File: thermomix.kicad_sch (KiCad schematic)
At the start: 30 parts, among them J101 DX07S016JA1R1500, J102 Conn_01x05, SW101 SW_Push, SW102 SW_Push, U101 MIC5353-3.3YMT, U102 TPD2E2U06, U103 STM32F303RDTx, Y101 Crystal_GND24

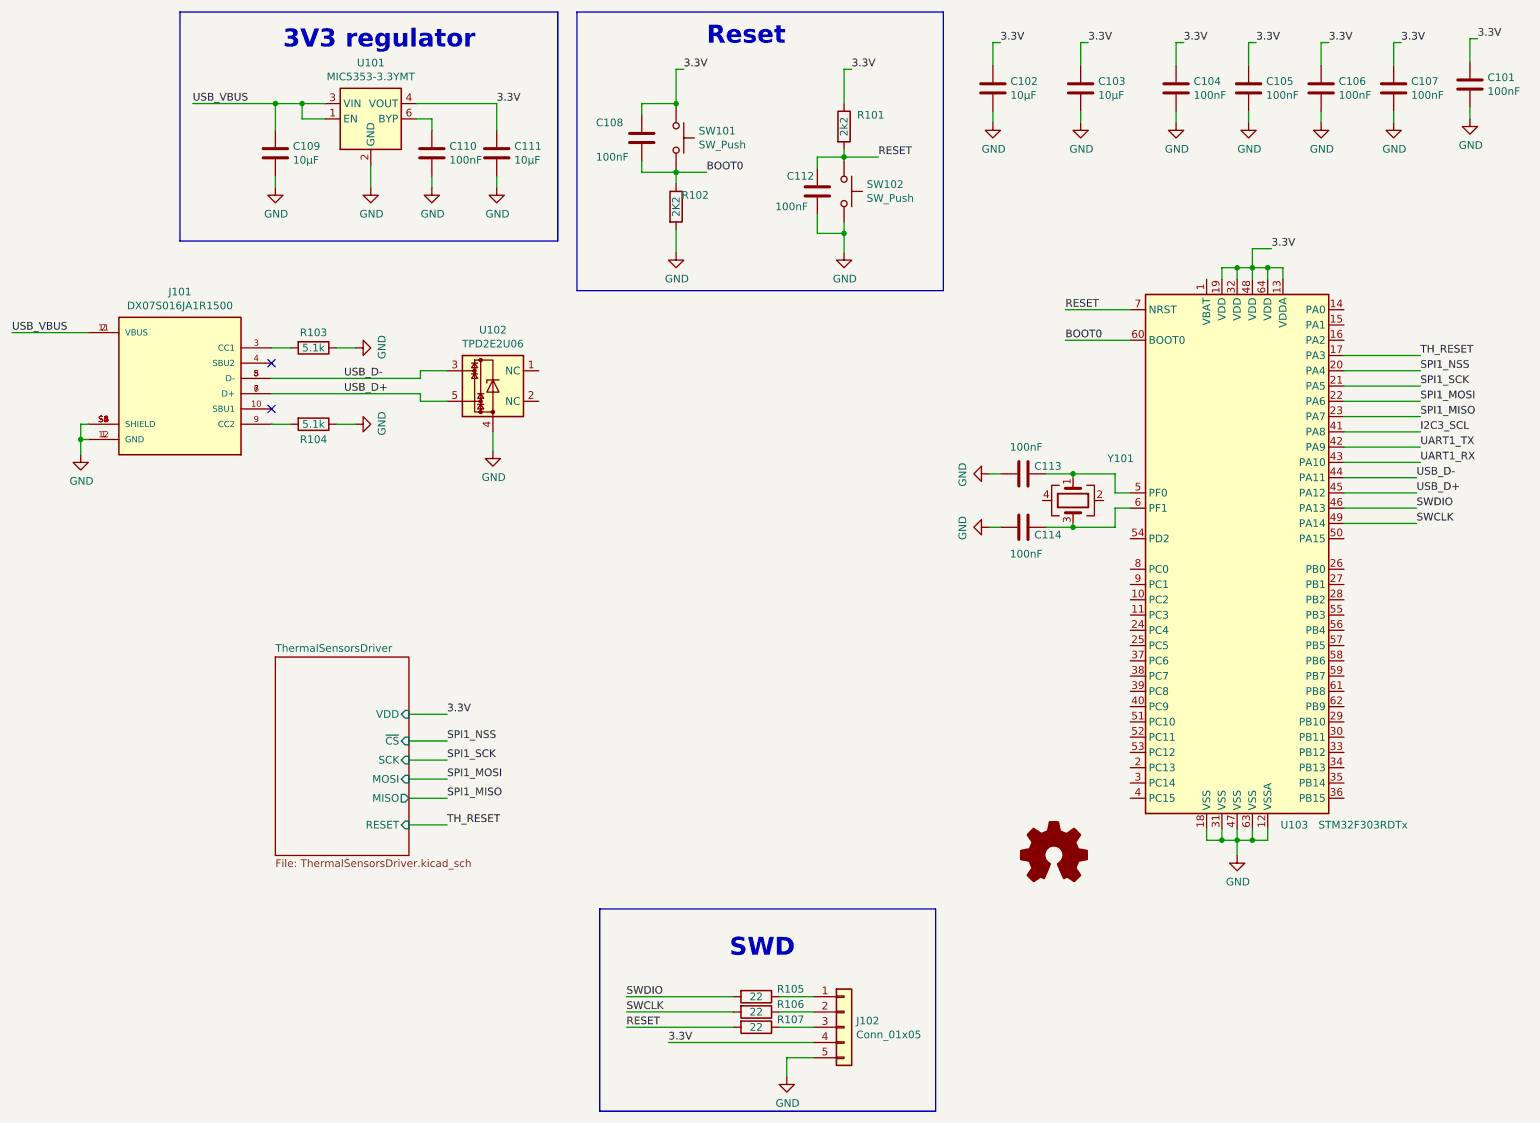
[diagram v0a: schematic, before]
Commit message: Adds sdcard and battery
Signed-off-by: Alexis Jeandet <alexis.jeandet@member.fsf.org>
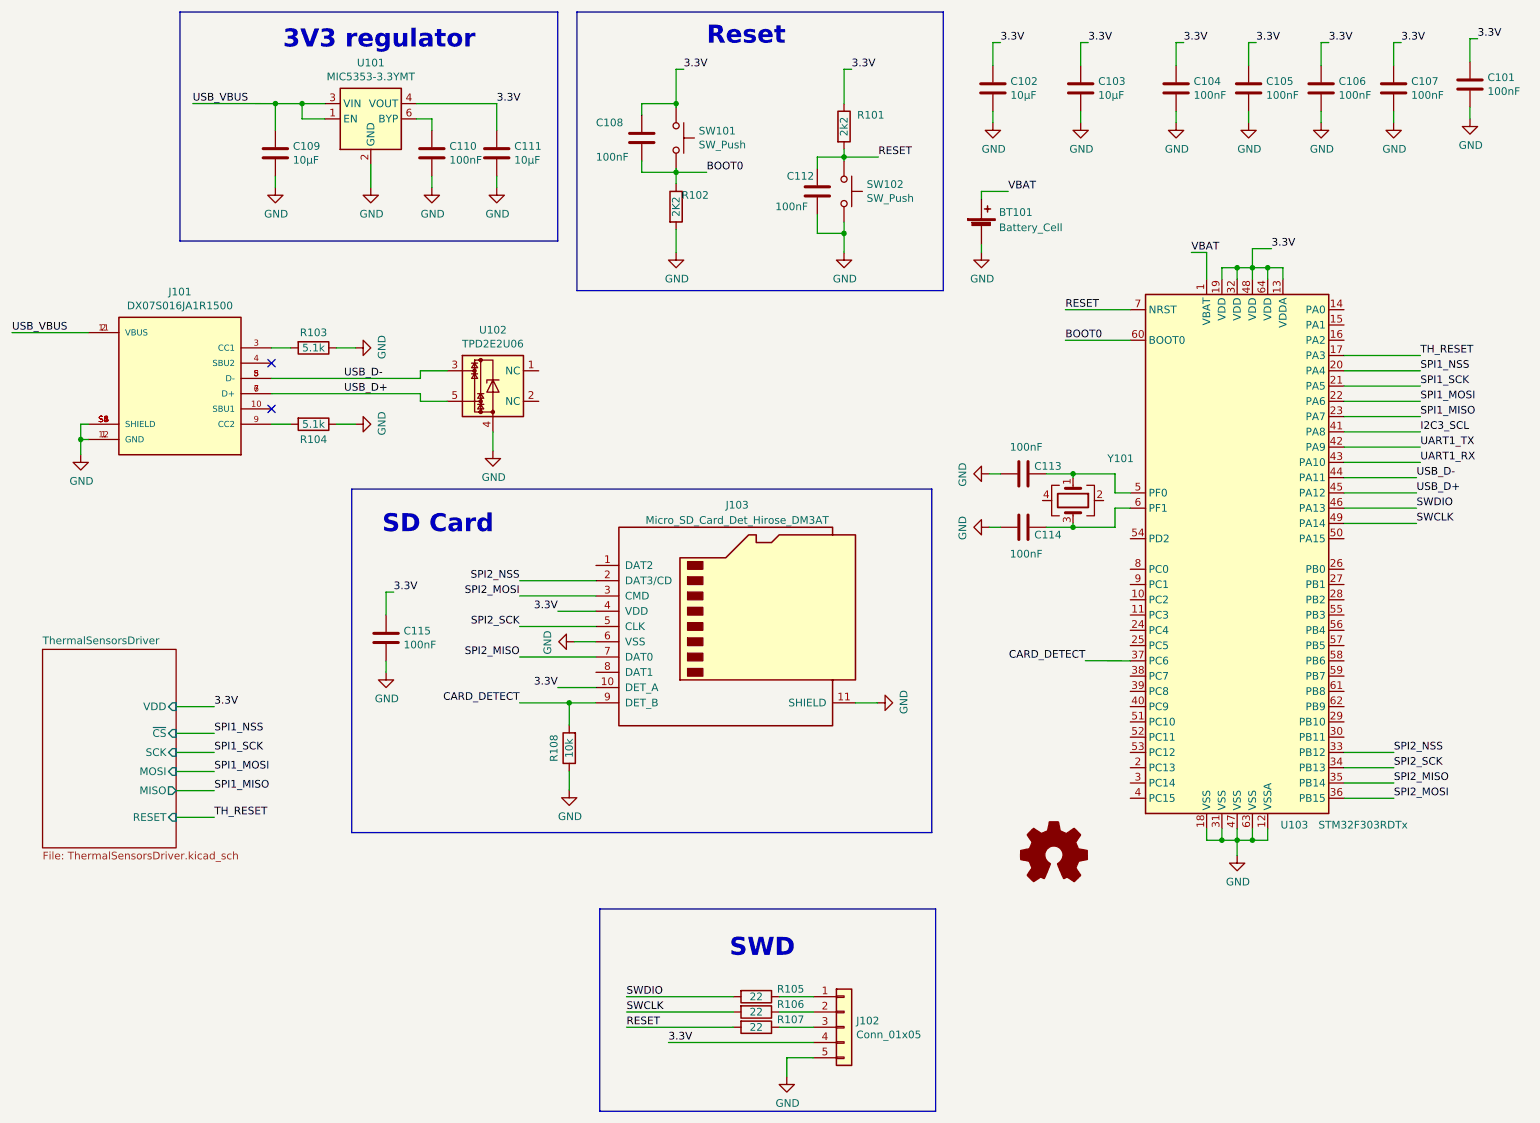
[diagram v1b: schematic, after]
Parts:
- added BT101: Battery_Cell, Battery:BatteryHolder_Keystone_3000_1x12mm, symbol Device:Battery_Cell
- added C115: 100nF, Capacitor_SMD:C_0603_1608Metric_Pad1.08x0.95mm_HandSolder, symbol Device:C
- added J103: Micro_SD_Card_Det_Hirose_DM3AT, Connector_Card:microSD_HC_Hirose_DM3D-SF, symbol Connector:Micro_SD_Card_Det_Hirose_DM3AT
- added R108: 10k, Resistor_SMD:R_0603_1608Metric_Pad0.98x0.95mm_HandSolder, symbol Device:R
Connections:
- net 3.3V: now also C115.1, J103.10 (DET_A), J103.4 (VDD)
- net GND: now also BT101.2 (-), C115.2, J103.11 (SHIELD), J103.6 (VSS), R108.1
- net VBAT: now reaches U103.1 (VBAT)
- net VBAT: now also BT101.1 (+)
- net SPI2_NSS: now reaches U103.33 (PB12)
- net SPI2_NSS: now also J103.2 (DAT3/CD)
- net SPI2_SCK: now reaches U103.34 (PB13)
- net SPI2_SCK: now also J103.5 (CLK)
- net SPI2_MISO: now reaches U103.35 (PB14)
- net SPI2_MISO: now also J103.7 (DAT0)
- net SPI2_MOSI: now reaches U103.36 (PB15)
- net SPI2_MOSI: now also J103.3 (CMD)
- net CARD_DETECT: now reaches U103.37 (PC6)
- net CARD_DETECT: now also J103.9 (DET_B), R108.2
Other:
- note added: "SD Card"

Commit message: 1.0 release
Signed-off-by: Alexis Jeandet <alexis.jeandet@member.fsf.org>
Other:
- company: (none) -> Laboratory of Plasma Physics
- title: (none) -> Thermomix
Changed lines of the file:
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@@
 (kicad_sch (version 20211123) (generator eeschema)
   (paper "A4")
+  (title_block
+    (title "Thermomix")
+    (date "2022-06-03")
+    (rev "1.0")
+    (company "Laboratory of Plasma Physics")
+    (comment 1 "Alexis Jeandet <alexis.jeandet@member.fsf.org>")
+  )
   (junction (at 132.715 29.845) (diameter 0) (color 0 0 0 0)
   )

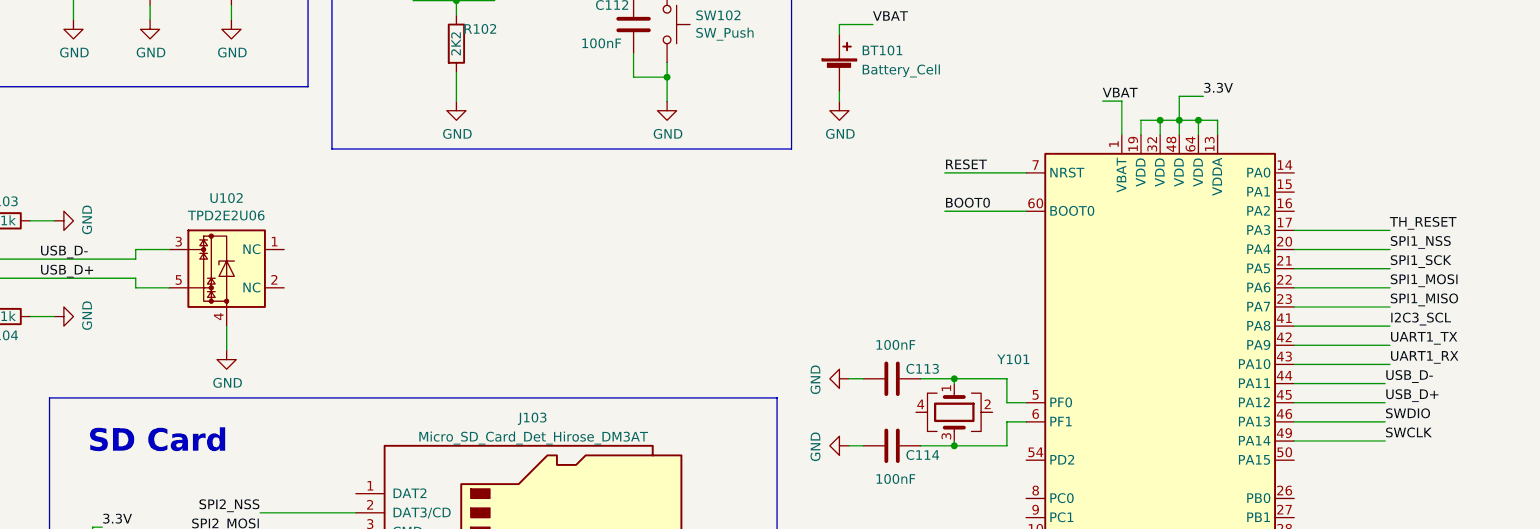
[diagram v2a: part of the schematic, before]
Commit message: Fixes bugs from 1.0
Signed-off-by: Alexis Jeandet <alexis.jeandet@member.fsf.org>
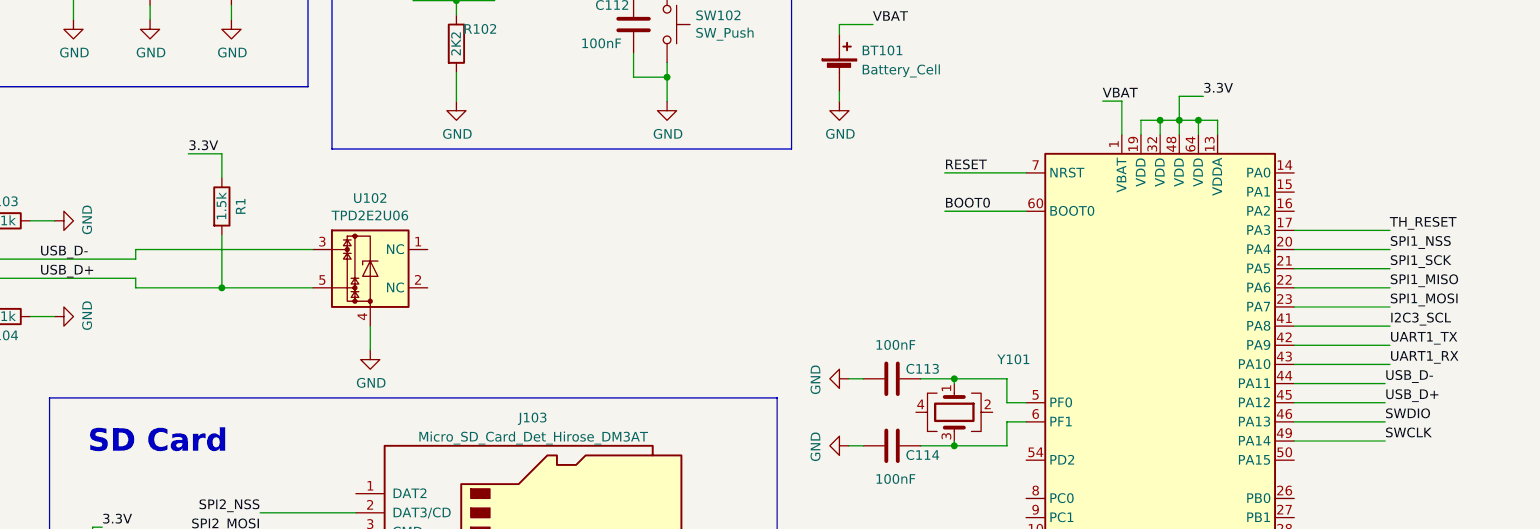
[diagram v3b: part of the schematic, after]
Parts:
- added R1: 1.5k, Resistor_SMD:R_0603_1608Metric_Pad0.98x0.95mm_HandSolder, symbol Device:R
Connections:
- net 3.3V: now also R1.1
- net SPI1_MISO: now also U103.22 (PA6); no longer U103.23 (PA7)
- net SPI1_MOSI: now also U103.23 (PA7); no longer U103.22 (PA6)
- net USB_D+: now also R1.2
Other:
- moved on the sheet: U102
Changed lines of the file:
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@@
     (title "Thermomix")
     (date "2022-06-03")
-    (rev "1.0")
+    (rev "1.1")
     (company "Laboratory of Plasma Physics")
     (comment 1 "Alexis Jeandet <alexis.jeandet@member.fsf.org>")
@@
   )
   (junction (at 231.14 57.15) (diameter 0) (color 0 0 0 0)
+  )
+  (junction (at 101.6 79.375) (diameter 0) (color 0 0 0 0)
   )
   (junction (at 228.6 152.4) (diameter 0) (color 0 0 0 0)
@@
     (stroke (width 0) (type default) (color 0 0 0 0))
   )
-  (wire (pts (xy 102.235 84.455) (xy 102.235 87.63))
+  (wire (pts (xy 121.285 84.455) (xy 121.285 87.63))
     (stroke (width 0) (type default) (color 0 0 0 0))
   )
@@
     (stroke (width 0) (type default) (color 0 0 0 0))
   )
+  (wire (pts (xy 101.6 72.39) (xy 101.6 79.375))
+    (stroke (width 0) (type default) (color 0 0 0 0))
+  )
   (wire (pts (xy 149.86 180.975) (xy 155.575 180.975))
     (stroke (width 0) (type default) (color 0 0 0 0))
@@
     (stroke (width 0) (type default) (color 0 0 0 0))
   )
-  (wire (pts (xy 94.615 79.375) (xy 90.17 79.375))
+  (wire (pts (xy 113.665 79.375) (xy 101.6 79.375))
     (stroke (width 0) (type default) (color 0 0 0 0))
   )
@@
     (stroke (width 0) (type default) (color 0 0 0 0))
   )
+  (wire (pts (xy 101.6 64.77) (xy 101.6 61.595))
+    (stroke (width 0) (type default) (color 0 0 0 0))
+  )
   (wire (pts (xy 227.965 19.685) (xy 227.965 23.495))
     (stroke (width 0) (type default) (color 0 0 0 0))
@@
     (stroke (width 0) (type default) (color 0 0 0 0))
   )
-  (wire (pts (xy 94.615 74.295) (xy 90.17 74.295))
+  (wire (pts (xy 113.665 74.295) (xy 90.17 74.295))
     (stroke (width 0) (type default) (color 0 0 0 0))
   )
@@
     (stroke (width 0) (type default) (color 0 0 0 0))
   )
+  (wire (pts (xy 101.6 61.595) (xy 97.155 61.595))
+    (stroke (width 0) (type default) (color 0 0 0 0))
+  )
   (wire (pts (xy 89.535 29.845) (xy 102.87 29.845))
+    (stroke (width 0) (type default) (color 0 0 0 0))
+  )
+  (wire (pts (xy 101.6 79.375) (xy 90.17 79.375))
     (stroke (width 0) (type default) (color 0 0 0 0))
   )
@@
     (effects (font (size 1.27 1.27)) (justify left bottom))
   )
-  (label "SPI1_MISO" (at 256.54 81.915 0)
+  (label "SPI1_MISO" (at 256.54 79.375 0)
     (effects (font (size 1.27 1.27)) (justify left bottom))
   )
@@
     (effects (font (size 1.27 1.27)) (justify left bottom))
   )
-  (label "SPI1_MOSI" (at 256.54 79.375 0)
+  (label "SPI1_MOSI" (at 256.54 81.915 0)
     (effects (font (size 1.27 1.27)) (justify left bottom))
   )
@@
   )
   (label "3.3V" (at 231.775 53.975 0)
+    (effects (font (size 1.27 1.27)) (justify left bottom))
+  )
+  (label "3.3V" (at 97.155 61.595 0)
     (effects (font (size 1.27 1.27)) (justify left bottom))
   )
@@
     )
     (property "Datasheet" "~" (id 3) (at 185.42 27.305 0)
+      (effects (font (size 1.27 1.27)) hide)
+    )
+    (pin "1")
+    (pin "2")
+  )
+  (symbol (lib_id "Device:R") (at 101.6 68.58 0) (unit 1)
+    (in_bom yes) (on_board yes)
+    (property "Reference" "R1" (id 0) (at 104.14 68.58 90))
+    (property "Value" "1.5k" (id 1) (at 101.6 68.58 90))
+    (property "Footprint" "Resistor_SMD:R_0603_1608Metric_Pad0.98x0.95mm_HandSolder" (id 2) (at 99.822 68.58 90)
+      (effects (font (size 1.27 1.27)) hide)
+    )
+    (property "Datasheet" "~" (id 3) (at 101.6 68.58 0)
       (effects (font (size 1.27 1.27)) hide)
     )
@@
     (pin "S6")
   )
-  (symbol (lib_id "Power_Protection:TPD2E2U06") (at 102.235 76.835 0) (unit 1)
-    (in_bom yes) (on_board yes)
-    (property "Reference" "U102" (id 0) (at 102.235 67.5132 0))
-    (property "Value" "TPD2E2U06" (id 1) (at 102.235 69.8246 0))
-    (property "Footprint" "Package_TO_SOT_SMD:SOT-553" (id 2) (at 81.915 83.185 0)
-      (effects (font (size 1.27 1.27)) hide)
-    )
-    (property "Datasheet" "http://www.ti.com/lit/ds/symlink/tpd2e2u06.pdf" (id 3) (at 97.155 71.755 0)
+  (symbol (lib_id "Power_Protection:TPD2E2U06") (at 121.285 76.835 0) (unit 1)
+    (in_bom yes) (on_board yes)
+    (property "Reference" "U102" (id 0) (at 121.285 67.5132 0))
+    (property "Value" "TPD2E2U06" (id 1) (at 121.285 69.8246 0))
+    (property "Footprint" "Package_TO_SOT_SMD:SOT-553" (id 2) (at 100.965 83.185 0)
+      (effects (font (size 1.27 1.27)) hide)
+    )
+    (property "Datasheet" "http://www.ti.com/lit/ds/symlink/tpd2e2u06.pdf" (id 3) (at 116.205 71.755 0)
       (effects (font (size 1.27 1.27)) hide)
     )
@@
     (pin "5")
   )
-  (symbol (lib_id "power:GND") (at 102.235 87.63 0) (unit 1)
-    (in_bom yes) (on_board yes)
-    (property "Reference" "#PWR0116" (id 0) (at 102.235 93.98 0)
-      (effects (font (size 1.27 1.27)) hide)
-    )
-    (property "Value" "GND" (id 1) (at 102.362 92.0242 0))
-    (property "Footprint" "" (id 2) (at 102.235 87.63 0)
-      (effects (font (size 1.27 1.27)) hide)
-    )
-    (property "Datasheet" "" (id 3) (at 102.235 87.63 0)
+  (symbol (lib_id "power:GND") (at 121.285 87.63 0) (unit 1)
+    (in_bom yes) (on_board yes)
+    (property "Reference" "#PWR0116" (id 0) (at 121.285 93.98 0)
+      (effects (font (size 1.27 1.27)) hide)
+    )
+    (property "Value" "GND" (id 1) (at 121.412 92.0242 0))
+    (property "Footprint" "" (id 2) (at 121.285 87.63 0)
+      (effects (font (size 1.27 1.27)) hide)
+    )
+    (property "Datasheet" "" (id 3) (at 121.285 87.63 0)
       (effects (font (size 1.27 1.27)) hide)
     )
@@
       (reference "LOGO101") (unit 1) (value "Logo_Open_Hardware_Small") (footprint "Symbol:KiCad-Logo2_5mm_SilkScreen")
     )
+    (path "/614c10de-d094-4afa-9ca6-f6b3303e4cae"
+      (reference "R1") (unit 1) (value "1.5k") (footprint "Resistor_SMD:R_0603_1608Metric_Pad0.98x0.95mm_HandSolder")
+    )
     (path "/8a3d03e2-f2c7-455f-8484-ae69e20feae4"
